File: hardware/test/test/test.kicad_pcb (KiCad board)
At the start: 2 copper layers, 1 part

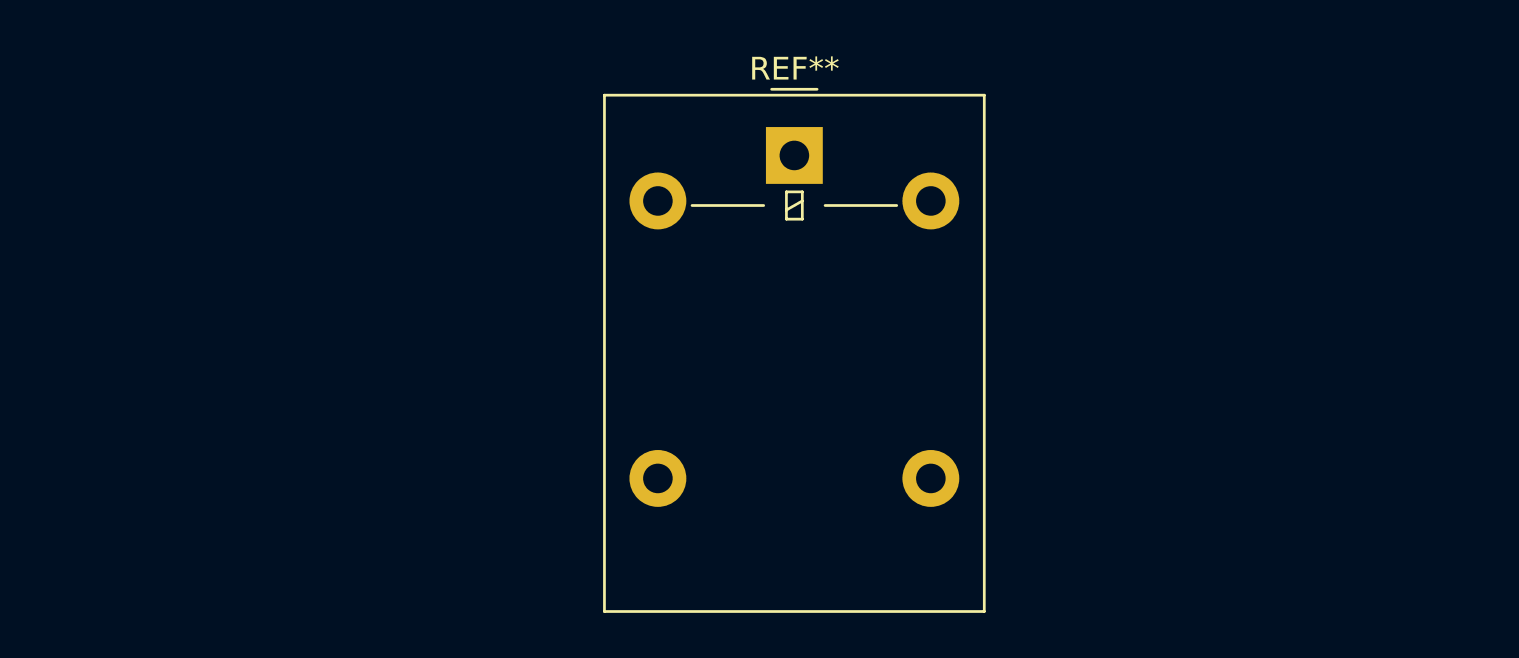
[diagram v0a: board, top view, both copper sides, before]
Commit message: Test for N-ch MOSFET 100A high end
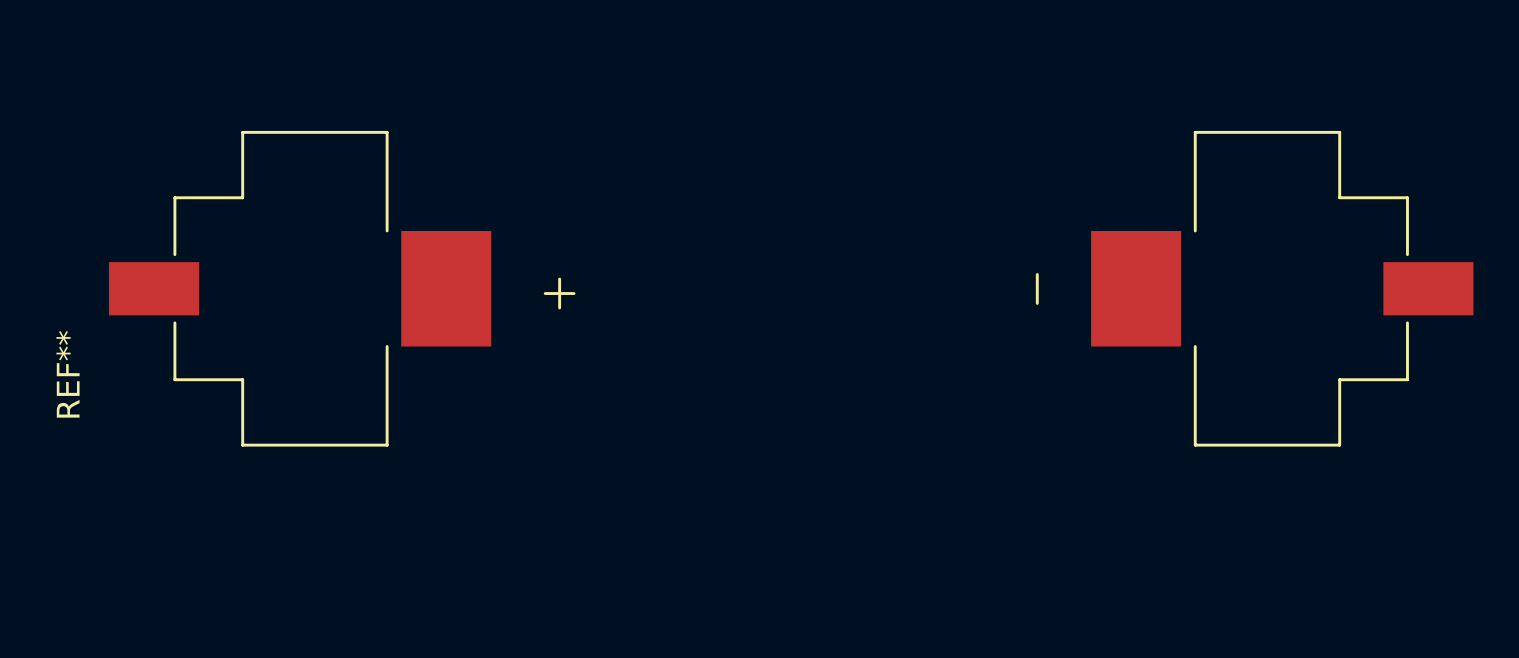
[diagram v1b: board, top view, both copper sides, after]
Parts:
- removed the REF** at (180.3, 91.4)
- added REF**: BAT_BK-53, BK-53:BAT_BK-53, F.Cu at (180.2, 97.3)
